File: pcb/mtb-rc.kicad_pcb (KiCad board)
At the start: 4 copper layers, 100 x 70 mm, 162 parts, among them J1 MVE252-5-V, J2 MVE252-5-V, J6 PINHEADER, J7 PINHEADER, J8 PROG/DEBUG, J9 MVE252-5-V, SW1 6x6, U1 VO0631T, U10 LM339, U11 LM339, U12 STM32F103C8Tx, U13 HT7533-1, U14 78M05, U15 MAX487, U2 VO0631T, U3 VO0631T, U4 L78L05_SOT89, U5 L79L05_SOT89, U6 LM339, U7 LM339, U8 LM339, U9 4052, Y1 14.7456MHz

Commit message: Remove "PAD" value of testpads where pads are not used.
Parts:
- TP1, TP10, TP11, TP12, TP2, TP3, TP4, TP5, TP6, TP7, TP8, TP9: value PAD -> ~
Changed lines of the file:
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@@
         (effects (font (size 1 1) (thickness 0.15)) (justify left))
     )
-    (fp_text value "PAD" (at 0 2.33) (layer "F.Fab")
+    (fp_text value "~" (at 0 2.33) (layer "F.Fab")
         (effects (font (size 1 1) (thickness 0.15)))
     )
@@
         (effects (font (size 1 1) (thickness 0.15)))
     )
-    (fp_text value "PAD" (at 0 2.33) (layer "F.Fab")
+    (fp_text value "~" (at 0 2.33) (layer "F.Fab")
         (effects (font (size 1 1) (thickness 0.15)))
     )
@@
         (effects (font (size 1 1) (thickness 0.15)))
     )
-    (fp_text value "PAD" (at 0 2.33) (layer "F.Fab")
+    (fp_text value "~" (at 0 2.33) (layer "F.Fab")
         (effects (font (size 1 1) (thickness 0.15)))
     )
@@
         (effects (font (size 1 1) (thickness 0.15)) (justify left))
     )
-    (fp_text value "PAD" (at 0 2.33) (layer "F.Fab")
+    (fp_text value "~" (at 0 2.33) (layer "F.Fab")
         (effects (font (size 1 1) (thickness 0.15)))
     )
@@
         (effects (font (size 1 1) (thickness 0.15)) (justify left))
     )
-    (fp_text value "PAD" (at 0 2.33) (layer "F.Fab")
+    (fp_text value "~" (at 0 2.33) (layer "F.Fab")
         (effects (font (size 1 1) (thickness 0.15)))
     )
@@
         (effects (font (size 1 1) (thickness 0.15)) (justify left))
     )
-    (fp_text value "PAD" (at 0 2.33) (layer "F.Fab")
+    (fp_text value "~" (at 0 2.33) (layer "F.Fab")
         (effects (font (size 1 1) (thickness 0.15)))
     )
@@
         (effects (font (size 1 1) (thickness 0.15)))
     )
-    (fp_text value "PAD" (at 0 2.33) (layer "F.Fab")
+    (fp_text value "~" (at 0 2.33) (layer "F.Fab")
         (effects (font (size 1 1) (thickness 0.15)))
     )
@@
         (effects (font (size 1 1) (thickness 0.15)) (justify left))
     )
-    (fp_text value "PAD" (at 0 2.33) (layer "F.Fab")
+    (fp_text value "~" (at 0 2.33) (layer "F.Fab")
         (effects (font (size 1 1) (thickness 0.15)))
     )
@@
         (effects (font (size 1 1) (thickness 0.15)))
     )
-    (fp_text value "PAD" (at 0 2.33) (layer "F.Fab")
+    (fp_text value "~" (at 0 2.33) (layer "F.Fab")
         (effects (font (size 1 1) (thickness 0.15)))
     )
@@
         (effects (font (size 1 1) (thickness 0.15)))
     )
-    (fp_text value "PAD" (at 0 2.33) (layer "F.Fab")
+    (fp_text value "~" (at 0 2.33) (layer "F.Fab")
         (effects (font (size 1 1) (thickness 0.15)))
     )
@@
         (effects (font (size 1 1) (thickness 0.15)))
     )
-    (fp_text value "PAD" (at 0 2.33) (layer "F.Fab")
+    (fp_text value "~" (at 0 2.33) (layer "F.Fab")
         (effects (font (size 1 1) (thickness 0.15)))
     )
@@
     (fp_arc (start 16.52 -3.485) (mid 16.698693 -2.993754) (end 16.475619 -2.521005)
       (stroke (width 0.1) (type solid)) (layer "F.Fab"))
-    (fp_arc (start 18.355426 -3.43) (mid 19.915165 -4.194874) (end 21.503665 -3.491686)
+    (fp_arc (start 18.355426 -3.43) (mid 19.915165 -4.194878) (end 21.503665 -3.491686)
       (stroke (width 0.1) (type solid)) (layer "F.Fab"))
     (fp_arc (start 18.555426 -2.56) (mid 18.253089 -2.981515) (end 18.4 -3.479005)
       (stroke (width 0.1) (type solid)) (layer "F.Fab"))
-    (fp_arc (start 21.495426 -2.55) (mid 19.99601 -2.064323) (end 18.513093 -2.598263)
+    (fp_arc (start 21.495426 -2.55) (mid 19.99601 -2.064325) (end 18.513093 -2.598263)
       (stroke (width 0.1) (type solid)) (layer "F.Fab"))
     (fp_arc (start 21.505426 -3.48) (mid 21.681152 -2.981652) (end 21.450958 -2.506005)
       (stroke (width 0.1) (type solid)) (layer "F.Fab"))
-    (fp_arc (start 23.363426 -3.385682) (mid 24.923165 -4.150555) (end 26.511665 -3.447368)
+    (fp_arc (start 23.363426 -3.385682) (mid 24.923165 -4.150559) (end 26.511665 -3.447368)
       (stroke (width 0.1) (type solid)) (layer "F.Fab"))
     (fp_arc (start 23.563426 -2.515682) (mid 23.264933 -2.945093) (end 23.420454 -3.444381)
       (stroke (width 0.1) (type solid)) (layer "F.Fab"))
-    (fp_arc (start 26.503426 -2.505682) (mid 25.00401 -2.020008) (end 23.521093 -2.553945)
+    (fp_arc (start 26.503426 -2.505682) (mid 25.00401 -2.02001) (end 23.521093 -2.553945)
       (stroke (width 0.1) (type solid)) (layer "F.Fab"))
     (fp_arc (start 26.513426 -3.435682) (mid 26.692099 -2.944442) (end 26.469045 -2.471687)
       (stroke (width 0.1) (type solid)) (layer "F.Fab"))
-    (fp_arc (start 28.343426 -3.37) (mid 29.903165 -4.134874) (end 31.491665 -3.431686)
+    (fp_arc (start 28.343426 -3.37) (mid 29.903165 -4.134878) (end 31.491665 -3.431686)
       (stroke (width 0.1) (type solid)) (layer "F.Fab"))
     (fp_arc (start 28.543426 -2.5) (mid 28.244946 -2.929406) (end 28.400454 -3.428699)
       (stroke (width 0.1) (type solid)) (layer "F.Fab"))
-    (fp_arc (start 31.483426 -2.49) (mid 29.984004 -2.004282) (end 28.501093 -2.538263)
+    (fp_arc (start 31.483426 -2.49) (mid 29.984004 -2.004262) (end 28.501093 -2.538263)
       (stroke (width 0.1) (type solid)) (layer "F.Fab"))
     (fp_arc (start 31.493426 -3.42) (mid 31.672112 -2.928754) (end 31.449045 -2.456005)
       (stroke (width 0.1) (type solid)) (layer "F.Fab"))
-    (fp_arc (start 33.373426 -3.355) (mid 34.933165 -4.119848) (end 36.521665 -3.416686)
+    (fp_arc (start 33.373426 -3.355) (mid 34.933165 -4.119852) (end 36.521665 -3.416686)
       (stroke (width 0.1) (type solid)) (layer "F.Fab"))
     (fp_arc (start 33.573426 -2.485) (mid 33.274946 -2.914406) (end 33.430454 -3.413699)
       (stroke (width 0.1) (type solid)) (layer "F.Fab"))
-    (fp_arc (start 36.513426 -2.475) (mid 35.014004 -1.989282) (end 33.531093 -2.523263)
+    (fp_arc (start 36.513426 -2.475) (mid 35.014004 -1.989262) (end 33.531093 -2.523263)
       (stroke (width 0.1) (type solid)) (layer "F.Fab"))
     (fp_arc (start 36.523426 -3.405) (mid 36.702112 -2.913754) (end 36.479045 -2.441005)
@@
         (effects (font (size 1 1) (thickness 0.15)) (justify left))
     )
-    (fp_text value "PAD" (at 0 2.33) (layer "F.Fab")
+    (fp_text value "~" (at 0 2.33) (layer "F.Fab")
         (effects (font (size 1 1) (thickness 0.15)))
     )

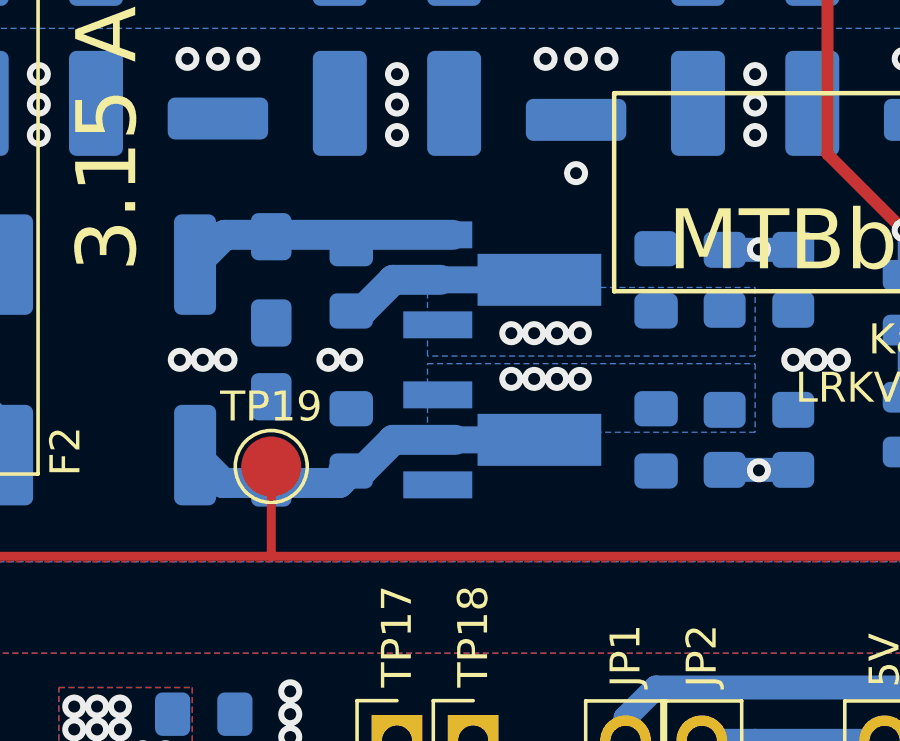
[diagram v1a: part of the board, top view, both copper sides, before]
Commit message: Use THT electrolytic capacitors for DCC stabilization.
22uF/25V tantalum capacitors are too big.
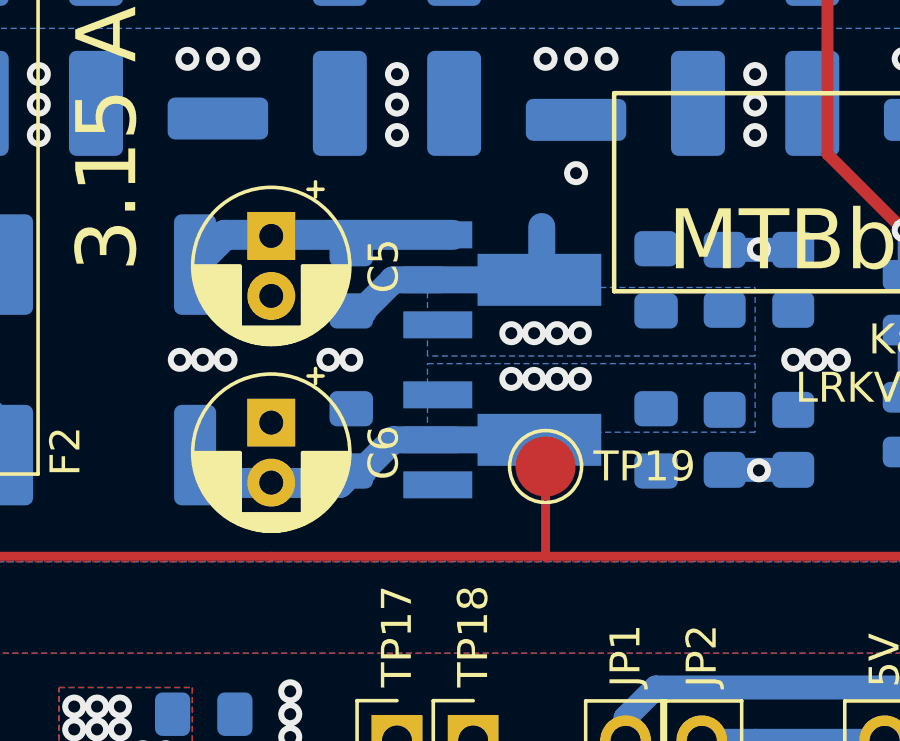
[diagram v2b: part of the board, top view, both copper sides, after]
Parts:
- C5, C6: value 22u -> 22u/25V; footprint Capacitor_Tantalum_SMD:CP_EIA-3216-10_Kemet-I_Pad1.58x1.35mm_HandSolder -> Capacitor_THT:CP_Radial_D5.0mm_P2.00mm; moved to F.Cu
- Y1: value 14.7456MHz -> 12MHz
- moved TP19 9.14 mm to (135.6, 62.9)
- moved C5 1.46 mm to (126.5, 55.2)
- moved C6 0.57 mm to (126.5, 61.4)
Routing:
- net GNDA: track 5.18 -> 6.75 mm

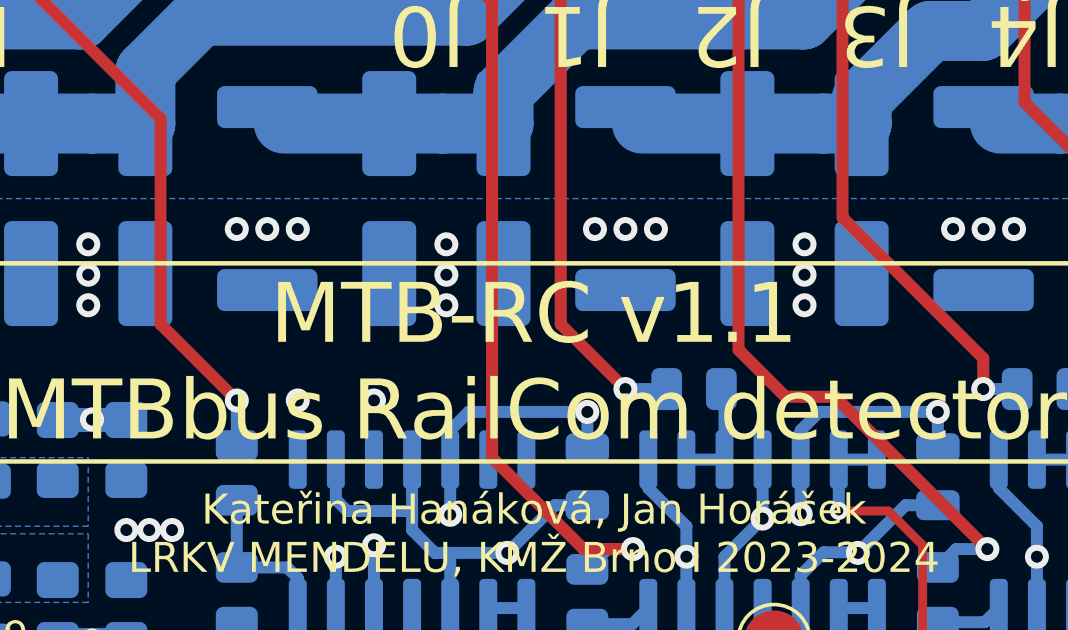
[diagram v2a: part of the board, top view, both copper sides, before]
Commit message: Fix RX/TX/TE silkscreen positions.
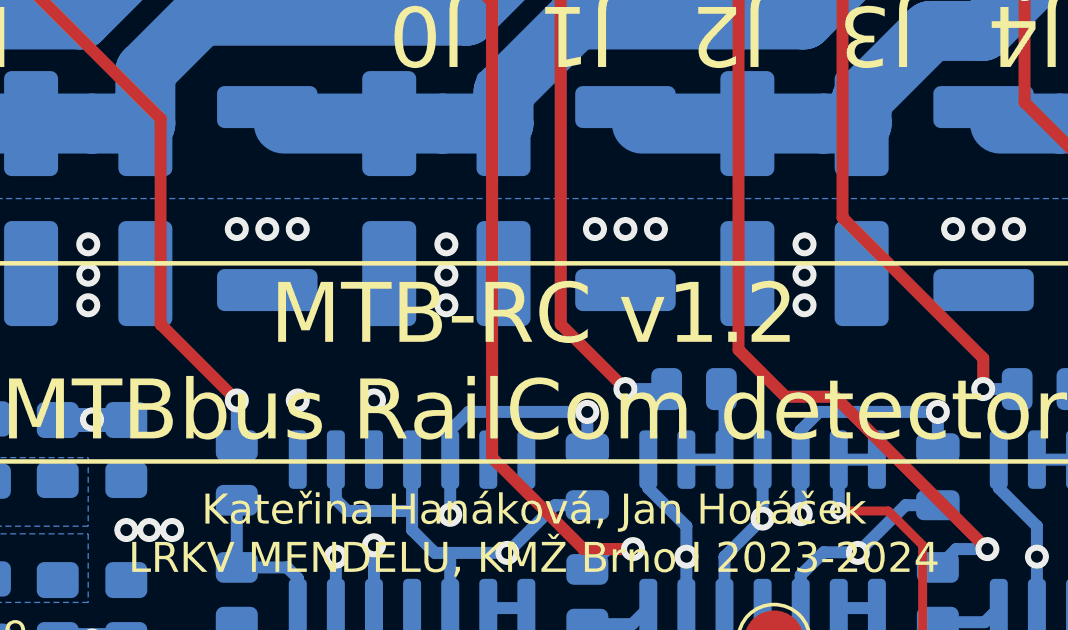
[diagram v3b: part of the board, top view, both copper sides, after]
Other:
- board text added: "MTB-RC v1.2 MTBbus RailCom detector"
- board text removed: "MTB-RC v1.1 MTBbus RailCom detector"
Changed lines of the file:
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@@
     (effects (font (size 0.9 0.9) (thickness 0.15)) (justify mirror))
   )
-  (gr_text "TE" (at 133.223 70.739) (layer "B.SilkS")
+  (gr_text "TE" (at 130.683 70.739) (layer "B.SilkS")
     (effects (font (size 1 1) (thickness 0.15)) (justify bottom mirror))
   )
@@
     (effects (font (size 0.8 0.8) (thickness 0.15)) (justify mirror))
   )
-  (gr_text "RX" (at 135.763 70.739) (layer "B.SilkS")
+  (gr_text "RX" (at 133.223 70.739) (layer "B.SilkS")
     (effects (font (size 1 1) (thickness 0.15)) (justify bottom mirror))
   )
@@
     (effects (font (size 0.8 0.8) (thickness 0.15)) (justify mirror))
   )
-  (gr_text "TX" (at 130.683 70.739) (layer "B.SilkS")
-    (effects (font (size 1 1) (thickness 0.15)) (justify bottom mirror))
+  (gr_text "TX" (at 131.826 74.549) (layer "B.SilkS")
+    (effects (font (size 1 1) (thickness 0.15)) (justify right mirror))
   )
   (gr_text "3.15 A" (at 113.919 51.816 90) (layer "F.SilkS")
@@
     (effects (font (size 2 2) (thickness 0.2)))
   )
-  (gr_text "MTB-RC v1.1\nMTBbus RailCom detector" (at 157.48 53.721) (layer "F.SilkS")
+  (gr_text "MTB-RC v1.2\nMTBbus RailCom detector" (at 157.48 53.721) (layer "F.SilkS")
     (effects (font (size 2 2) (thickness 0.25)))
   )

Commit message: R28 1k -> 4k7 (LED).
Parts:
- R28: value 1k -> 4k7
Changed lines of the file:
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@@
         (effects (font (size 1 1) (thickness 0.15)) (justify mirror))
     )
-    (fp_text value "1k" (at 0 -1.65) (layer "B.Fab")
+    (fp_text value "4k7" (at 0 -1.65) (layer "B.Fab")
         (effects (font (size 1 1) (thickness 0.15)) (justify mirror))
     )

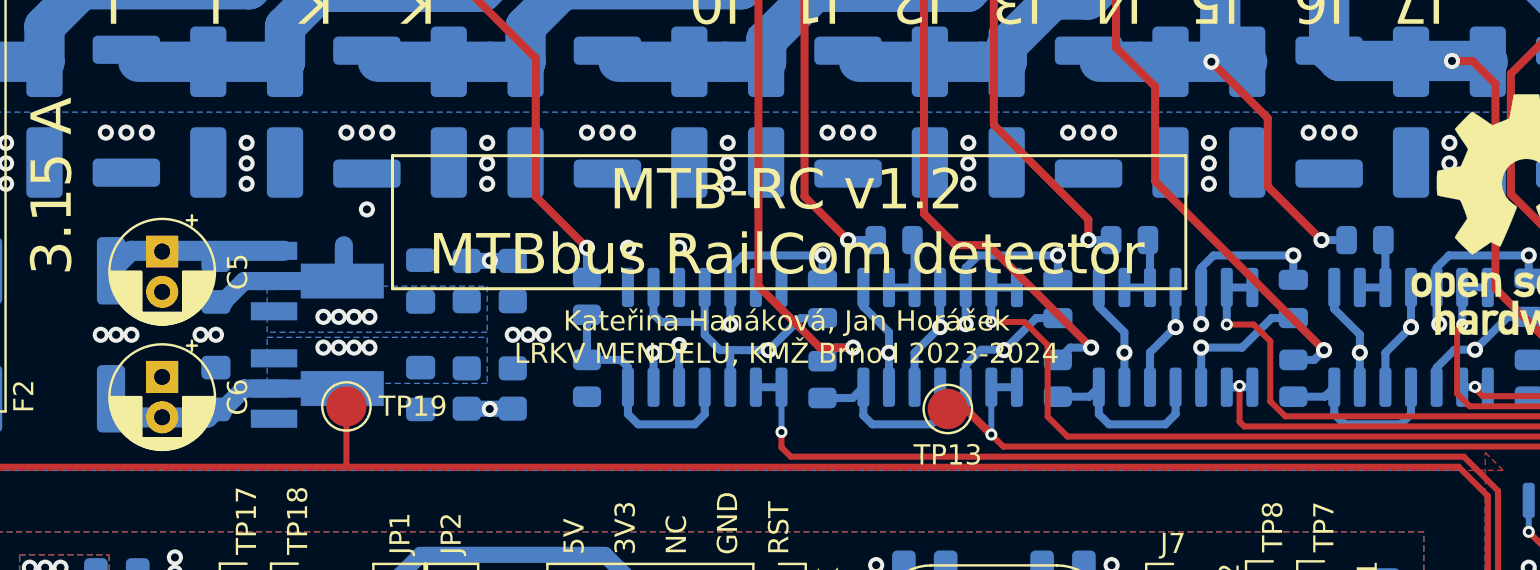
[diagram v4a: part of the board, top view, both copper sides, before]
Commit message: Add REF+/- capacitors C30, C31, C32, C33.
These capacitors filter out any disturbances in REF+ & REF- signals.
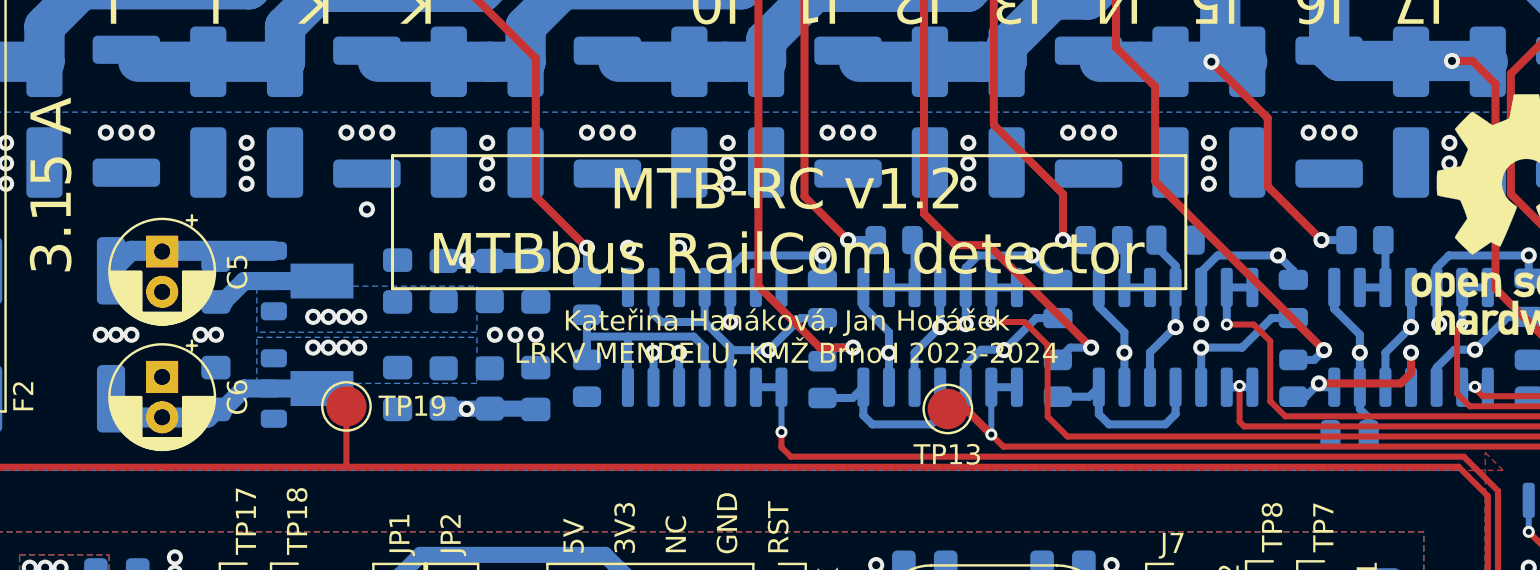
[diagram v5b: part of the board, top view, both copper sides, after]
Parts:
- added C30: 100n, Capacitor_SMD:C_0805_2012Metric_Pad1.18x1.45mm_HandSolder, B.Cu at (145.0, 56.6)
- added C31: 100n, Capacitor_SMD:C_0805_2012Metric, B.Cu at (176.8, 54.6)
- added C32: 100n, Capacitor_SMD:C_0805_2012Metric_Pad1.18x1.45mm_HandSolder, B.Cu at (145.0, 62.0)
- added C33: 100n, Capacitor_SMD:C_0805_2012Metric, B.Cu at (185.4, 64.3)
- U4, U5: footprint Package_TO_SOT_SMD:SOT-89-3_Handsoldering -> Package_TO_SOT_SMD:SOT-89-3
- moved R23 1.27 mm to (173.2, 54.6)
- moved C10 1.14 mm to (138.2, 62.0)
- moved C9 1.14 mm to (138.2, 56.6)
- moved R24 1.14 mm to (140.5, 56.6)
- moved R25 1.14 mm to (142.7, 56.6)
- moved R26 1.14 mm to (142.7, 62.0)
- moved R27 1.14 mm to (140.5, 62.0)
- moved U4 0.51 mm to (134.0, 56.6)
- moved U5 0.51 mm to (134.0, 62.0)
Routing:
- net REF+: track 93.1 -> 99.3 mm
- net REF-: track 93.1 -> 99.1 mm
- net GNDA: track 6.75 -> 5.18 mm
- net -5VA: track 50.2 -> 48.8 mm
- net Net-(U8A--): track 9.13 -> 9.89 mm, vias 0 -> 2
- net /DCC/J3: track 43.8 -> 43.3 mm
- net Net-(U5-VI): track 9.81 -> 9.30 mm
- net Net-(U4-IN): track 9.00 -> 8.49 mm
